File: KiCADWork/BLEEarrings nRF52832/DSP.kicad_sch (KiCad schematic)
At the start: 26 parts, among them J1 Screw_Terminal_01x01, J2 Screw_Terminal_01x02, U2 nRF52832-QFxx, Y1 Crystal_GND23

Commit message: Small Bits
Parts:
- added C14: 100n, Capacitor_SMD:C_0402_1005Metric_Pad0.74x0.62mm_HandSolder, symbol Device:C
- added C15, C16: 16p, Capacitor_SMD:C_0402_1005Metric_Pad0.74x0.62mm_HandSolder, symbol Device:C
- added R8: 2k, Resistor_SMD:R_0402_1005Metric_Pad0.72x0.64mm_HandSolder, symbol Device:R
- added SW2: SW_DIP_x01, easyeda2kicad:KEY-SMD_L3.0-W2.5-LS4.0, symbol Switch:SW_DIP_x01
- added Y2: Crystal, easyeda2kicad:CRYSTAL-SMD_L1.6-W1.0, symbol Device:Crystal
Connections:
- net +3V3: now also R8.2
- net GND: now also C3.1, C4.1, C14.1, C15.1, C16.1, SW2.2; no longer C3.2, C4.2
- net at U2.34 (XC1), Y1.4: now also C3.2; no longer C3.1
- net at U2.35 (XC2), Y1.1: now also C4.2; no longer C4.1
- net at U2.2 (P0.00/XL1): now also C15.2, Y2.2
- net at U2.3 (P0.01/XL2): now also C16.2, Y2.1
- net at U2.42 (P0.30/AIN6): now also C14.2, R8.1, SW2.1
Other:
- moved on the sheet: C3, C4, J1, J2, R5, TP4

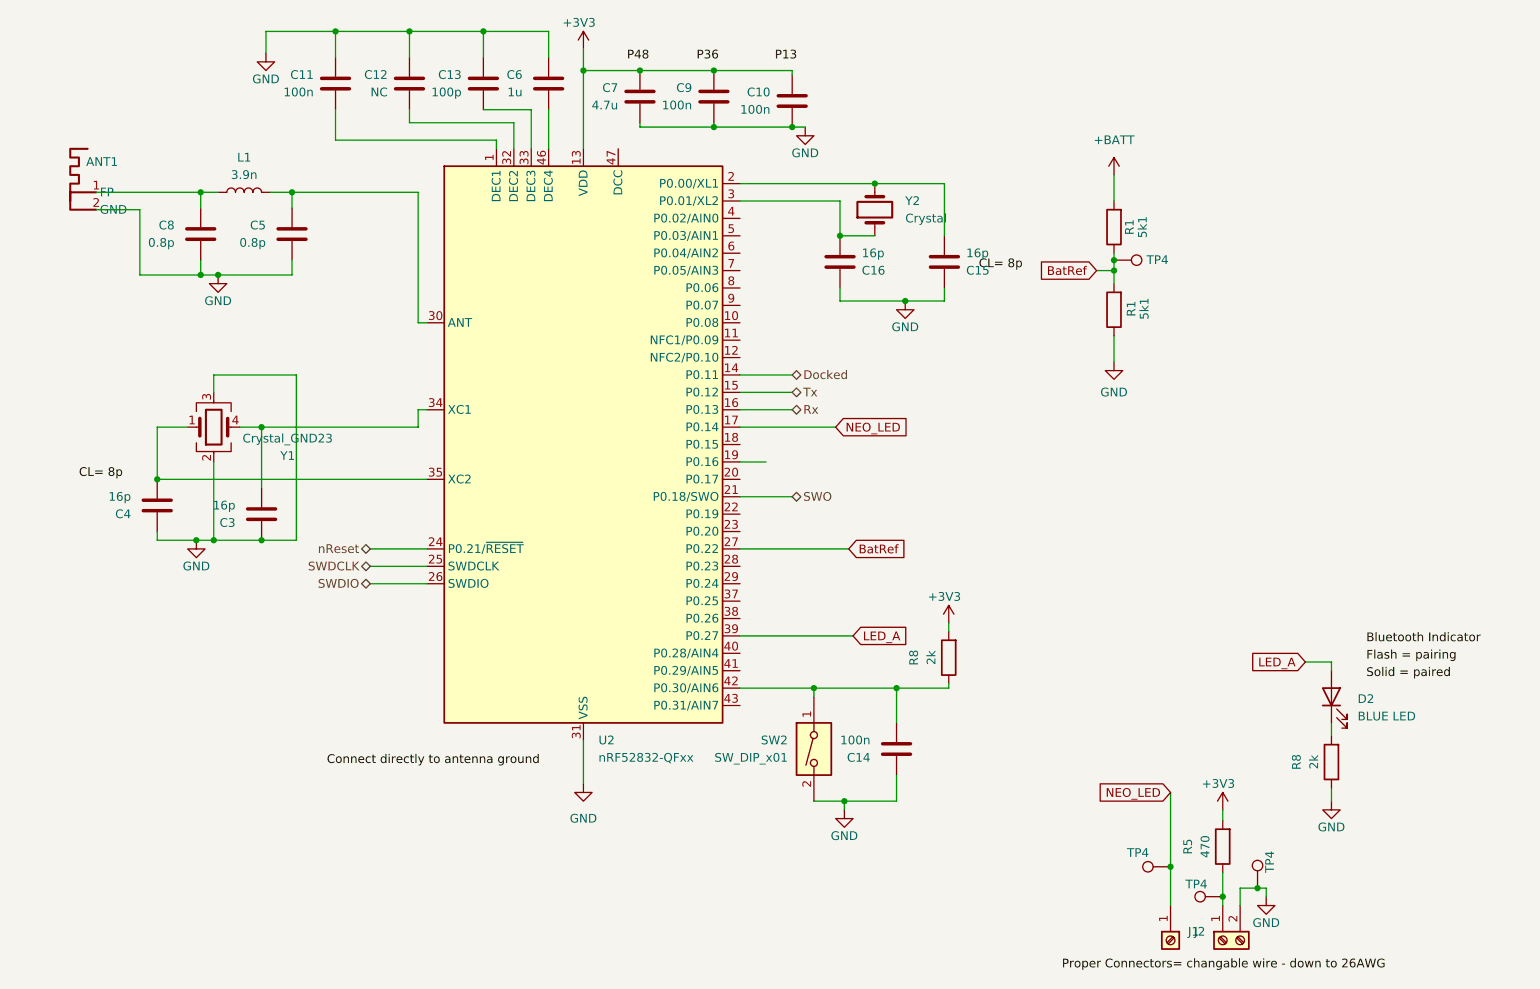
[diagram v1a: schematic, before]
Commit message: New Chip NRF52833
large changes
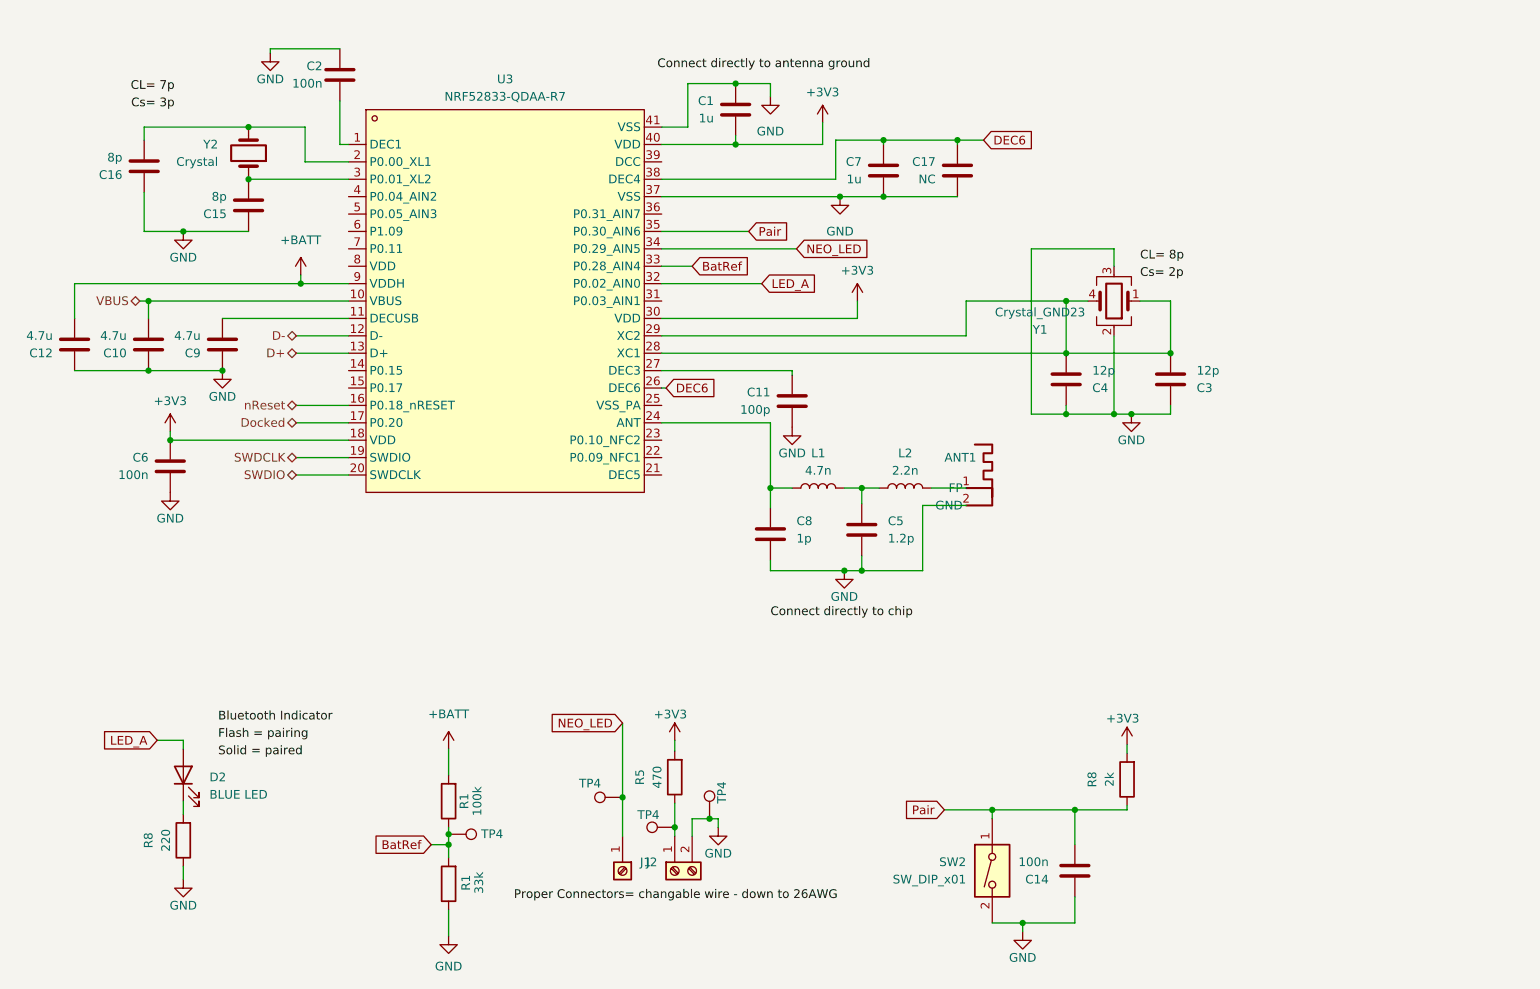
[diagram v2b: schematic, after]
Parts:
- removed C13: 100p, Capacitor_SMD:C_0402_1005Metric_Pad0.74x0.62mm_HandSolder, symbol Device:C
- removed U2: nRF52832-QFxx, Package_DFN_QFN:QFN-48-1EP_6x6mm_P0.4mm_EP4.6x4.6mm, symbol MCU_Nordic:nRF52832-QFxx
- added C1: 1u, Capacitor_SMD:C_0402_1005Metric_Pad0.74x0.62mm_HandSolder, symbol Device:C
- added C17: NC, Capacitor_SMD:C_0402_1005Metric_Pad0.74x0.62mm_HandSolder, symbol Device:C
- added C2: 100n, Capacitor_SMD:C_0402_1005Metric_Pad0.74x0.62mm_HandSolder, symbol Device:C
- added L2: 2.2n, Inductor_SMD:L_0402_1005Metric_Pad0.77x0.64mm_HandSolder, symbol Device:L
- added U3: NRF52833-QDAA-R7, easyeda2kicad:QFN-40_L5.0-W5.0-P0.40-TL-EP3.6, symbol easyeda2kicad:NRF52833-QDAA-R7
- C10, C9: value 100n -> 4.7u
- C11: value 100n -> 100p
- C12: value NC -> 4.7u
- C15, C16: value 16p -> 8p
- C3, C4: value 16p -> 12p
- C5: value 0.8p -> 1.2p
- C6: value 1u -> 100n
- C7: value 4.7u -> 1u
- C8: value 0.8p -> 1p
- L1: value 3.9n -> 4.7n
- R1: value 5k1 -> 33k
- R1: value 5k1 -> 100k
- R8: value 2k -> 220
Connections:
- net +3V3: now also C6.1, C1.2, U3.18 (VDD), U3.30 (VDD), U3.40 (VDD); no longer C10.2, C7.1, C9.2
- net +BATT: now also C12.2, U3.9 (VDDH)
- net BatRef: now also U3.33 (P0.28_AIN4)
- net Docked: now also U3.17 (P0.20)
- net GND: now also C11.2, C6.2, C1.1, C17.2, C2.1, U3.37 (VSS), U3.41 (VSS); no longer C11.1, C6.1
- net LED_A: now also U3.32 (P0.02_AIN0)
- net NEO_LED: now also U3.34 (P0.29_AIN5)
- net SWDCLK: now also U3.19 (SWDIO)
- net SWDIO: now also U3.20 (SWDCLK)
- net nReset: now also U3.16 (P0.18_nRESET)
- net at C15.2: now also Y2.1, U3.3 (P0.01_XL2); no longer Y2.2
- net at C5.1: now also L1.2, L2.1; no longer L1.1
- net at C3.2, Y1.4: now also C4.2, Y1.1, U3.28 (XC1), U3.29 (XC2)
- net Pair: now reaches C14.2, R8.1, SW2.1
- net Pair: now also U3.35 (P0.30_AIN6)
- net at C16.2: now also Y2.2, U3.2 (P0.00_XL1); no longer Y2.1
- new net: C8.1, L1.1, U3.24 (ANT)
- new net: ANT1.1 (FP), L2.2
- new net: C9.2, U3.11 (DECUSB)
- new net: C2.2, U3.1 (DEC1)
- new net: C11.1, U3.27 (DEC3)
- new net D+: U3.13 (D+)
- new net D-: U3.12 (D-)
- new net DEC6: C17.1, C7.1, U3.26 (DEC6), U3.38 (DEC4)
- new net VBUS: C10.2, U3.10 (VBUS)
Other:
- moved on the sheet: D2, J1, J2, R1, R5, R8, TP4

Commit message: Dock Updates
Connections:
- net Docked renamed SWO
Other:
- moved on the sheet: C14, R8, SW2

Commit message: Dock Updates
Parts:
- Y1: value Crystal_GND23 -> XL7EL89CKI-111YLC-32M
- Y2: value Crystal -> X161032768KLD2SI
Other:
- moved on the sheet: C16
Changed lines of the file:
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@@
     (stroke (width 0) (type default))
   )
-  (wire (pts (xy 34.925 40.005) (xy 34.925 41.91))
+  (wire (pts (xy 23.495 40.005) (xy 23.495 41.91))
     (stroke (width 0) (type default))
   )
@@
     (stroke (width 0) (type default))
   )
-  (wire (pts (xy 34.925 40.005) (xy 50.165 40.005))
+  (wire (pts (xy 23.495 40.005) (xy 50.165 40.005))
     (stroke (width 0) (type default))
   )
@@
     (stroke (width 0) (type default))
   )
-  (wire (pts (xy 34.925 55.245) (xy 34.925 49.53))
+  (wire (pts (xy 23.495 55.245) (xy 23.495 49.53))
     (stroke (width 0) (type default))
   )
@@
     (stroke (width 0) (type default))
   )
-  (wire (pts (xy 40.64 55.245) (xy 34.925 55.245))
+  (wire (pts (xy 40.64 55.245) (xy 23.495 55.245))
     (stroke (width 0) (type default))
   )
@@
     (stroke (width 0) (type default))
   )
-  (label "CL= 7p" (at 39.37 34.925 180) (fields_autoplaced)
-    (effects (font (size 1.27 1.27)) (justify right bottom))
-  )
-  (label "Cs= 3p" (at 39.37 37.465 180) (fields_autoplaced)
-    (effects (font (size 1.27 1.27)) (justify right bottom))
+  (label "CL= 7p" (at 27.305 35.56 0) (fields_autoplaced)
+    (effects (font (size 1.27 1.27)) (justify left bottom))
+  )
+  (label "Cs= 3p" (at 27.305 38.1 0) (fields_autoplaced)
+    (effects (font (size 1.27 1.27)) (justify left bottom))
   )
   (label "Connect directly to chip" (at 126.365 111.76 0) (fields_autoplaced)
     (effects (font (size 1.27 1.27)) (justify left bottom))
   )
-  (label "Cs= 2p" (at 180.34 62.23 0) (fields_autoplaced)
+  (label "Cs= 2p" (at 172.085 56.515 0) (fields_autoplaced)
     (effects (font (size 1.27 1.27)) (justify left bottom))
   )
@@
     (effects (font (size 1.27 1.27)) (justify left bottom))
   )
+  (label "32.768kHz Clock" (at 27.305 33.02 0) (fields_autoplaced)
+    (effects (font (size 1.27 1.27)) (justify left bottom))
+  )
   (label "Connect directly to antenna ground" (at 109.855 31.75 0) (fields_autoplaced)
     (effects (font (size 1.27 1.27)) (justify left bottom))
   )
-  (label "CL= 8p" (at 180.34 59.69 0) (fields_autoplaced)
+  (label "CL= 8p" (at 172.085 53.975 0) (fields_autoplaced)
+    (effects (font (size 1.27 1.27)) (justify left bottom))
+  )
+  (label "32MHz clock" (at 172.085 51.435 0) (fields_autoplaced)
     (effects (font (size 1.27 1.27)) (justify left bottom))
   )
@@
       (effects (font (size 1.27 1.27)) (justify right))
     )
-    (property "Value" "Crystal" (at 45.72 45.085 90)
+    (property "Value" " X161032768KLD2SI" (at 45.72 45.085 90)
       (effects (font (size 1.27 1.27)) (justify right))
     )
@@
     )
   )
-  (symbol (lib_id "Device:C") (at 34.925 45.72 180) (unit 1)
-    (in_bom yes) (on_board yes) (dnp no)
-    (property "Reference" "C16" (at 31.75 46.99 0)
-      (effects (font (size 1.27 1.27)) (justify left))
-    )
-    (property "Value" "8p" (at 31.75 44.45 0)
-      (effects (font (size 1.27 1.27)) (justify left))
-    )
-    (property "Footprint" "Capacitor_SMD:C_0402_1005Metric_Pad0.74x0.62mm_HandSolder" (at 33.9598 41.91 0)
-      (effects (font (size 1.27 1.27)) hide)
-    )
-    (property "Datasheet" "~" (at 34.925 45.72 0)
+  (symbol (lib_id "Device:C") (at 23.495 45.72 180) (unit 1)
+    (in_bom yes) (on_board yes) (dnp no)
+    (property "Reference" "C16" (at 20.32 46.99 0)
+      (effects (font (size 1.27 1.27)) (justify left))
+    )
+    (property "Value" "8p" (at 20.32 44.45 0)
+      (effects (font (size 1.27 1.27)) (justify left))
+    )
+    (property "Footprint" "Capacitor_SMD:C_0402_1005Metric_Pad0.74x0.62mm_HandSolder" (at 22.5298 41.91 0)
+      (effects (font (size 1.27 1.27)) hide)
+    )
+    (property "Datasheet" "~" (at 23.495 45.72 0)
       (effects (font (size 1.27 1.27)) hide)
     )
@@
   )
   (symbol (lib_id "Device:Crystal_GND23") (at 176.53 65.405 180) (unit 1)
-    (in_bom yes) (on_board yes) (dnp no) (fields_autoplaced)
-    (property "Reference" "Y1" (at 165.735 69.5959 0)
-      (effects (font (size 1.27 1.27)))
-    )
-    (property "Value" "Crystal_GND23" (at 165.735 67.0559 0)
-      (effects (font (size 1.27 1.27)))
-    )
+    (in_bom yes) (on_board yes) (dnp no)
+    (property "Reference" "Y1" (at 182.245 63.5 0)
+      (effects (font (size 1.27 1.27)))
+    )
+    (property "Value" "XL7EL89CKI-111YLC-32M " (at 193.675 60.96 0)
+      (effects (font (size 1.27 1.27)))
+    )

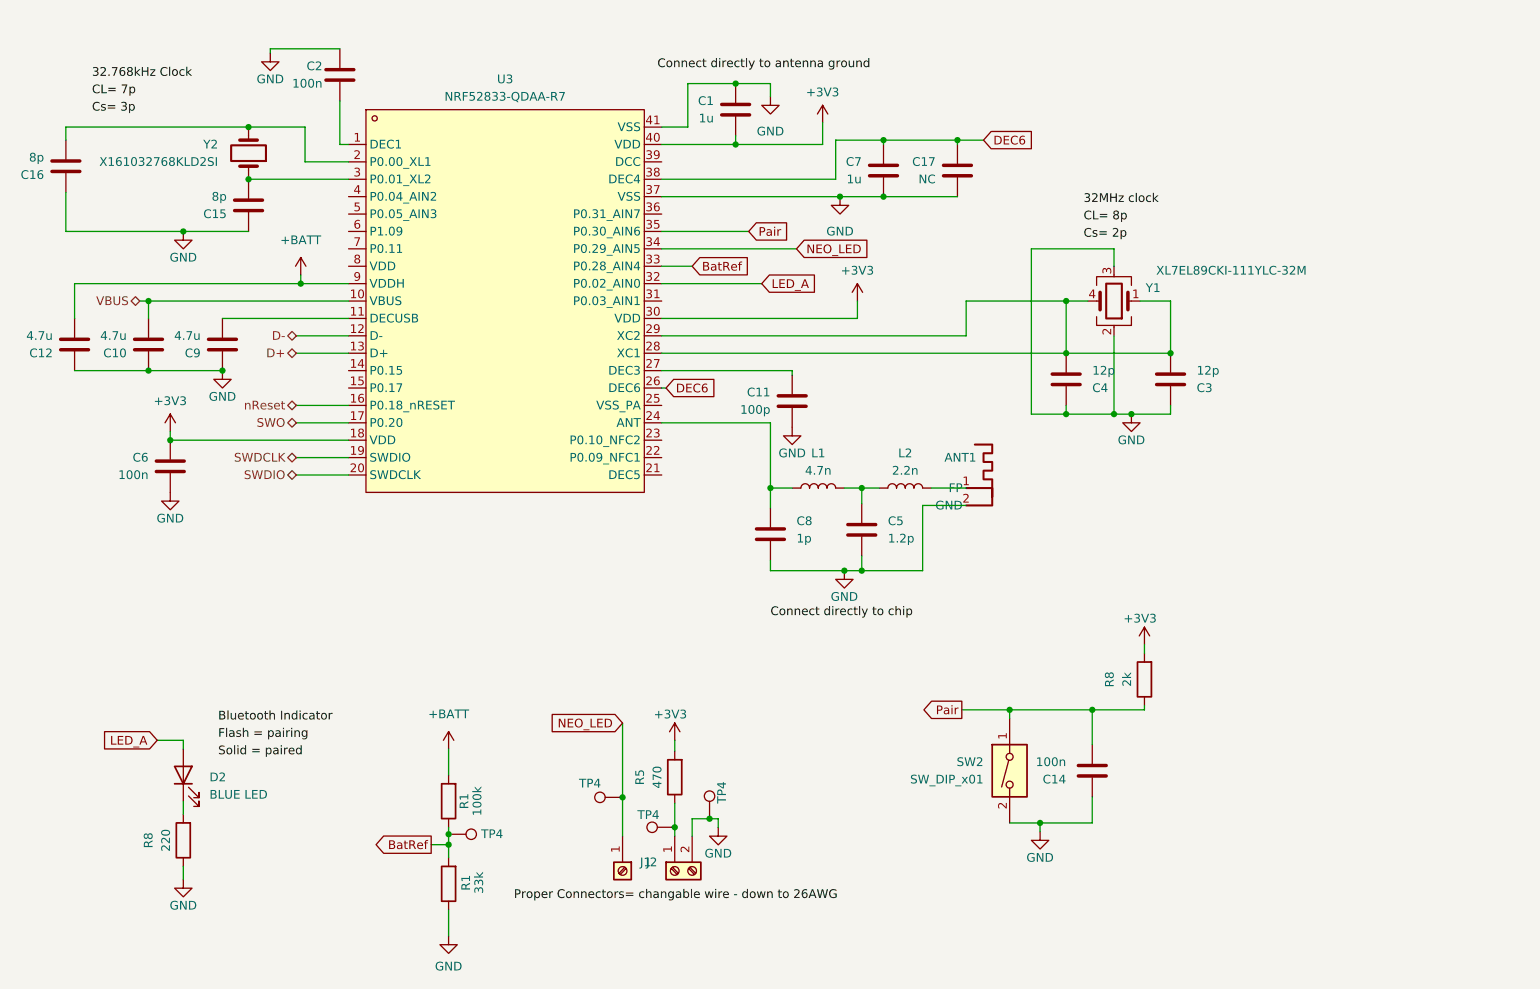
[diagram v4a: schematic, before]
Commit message: Routing Started on Earrings Again
- Only small routing changes made
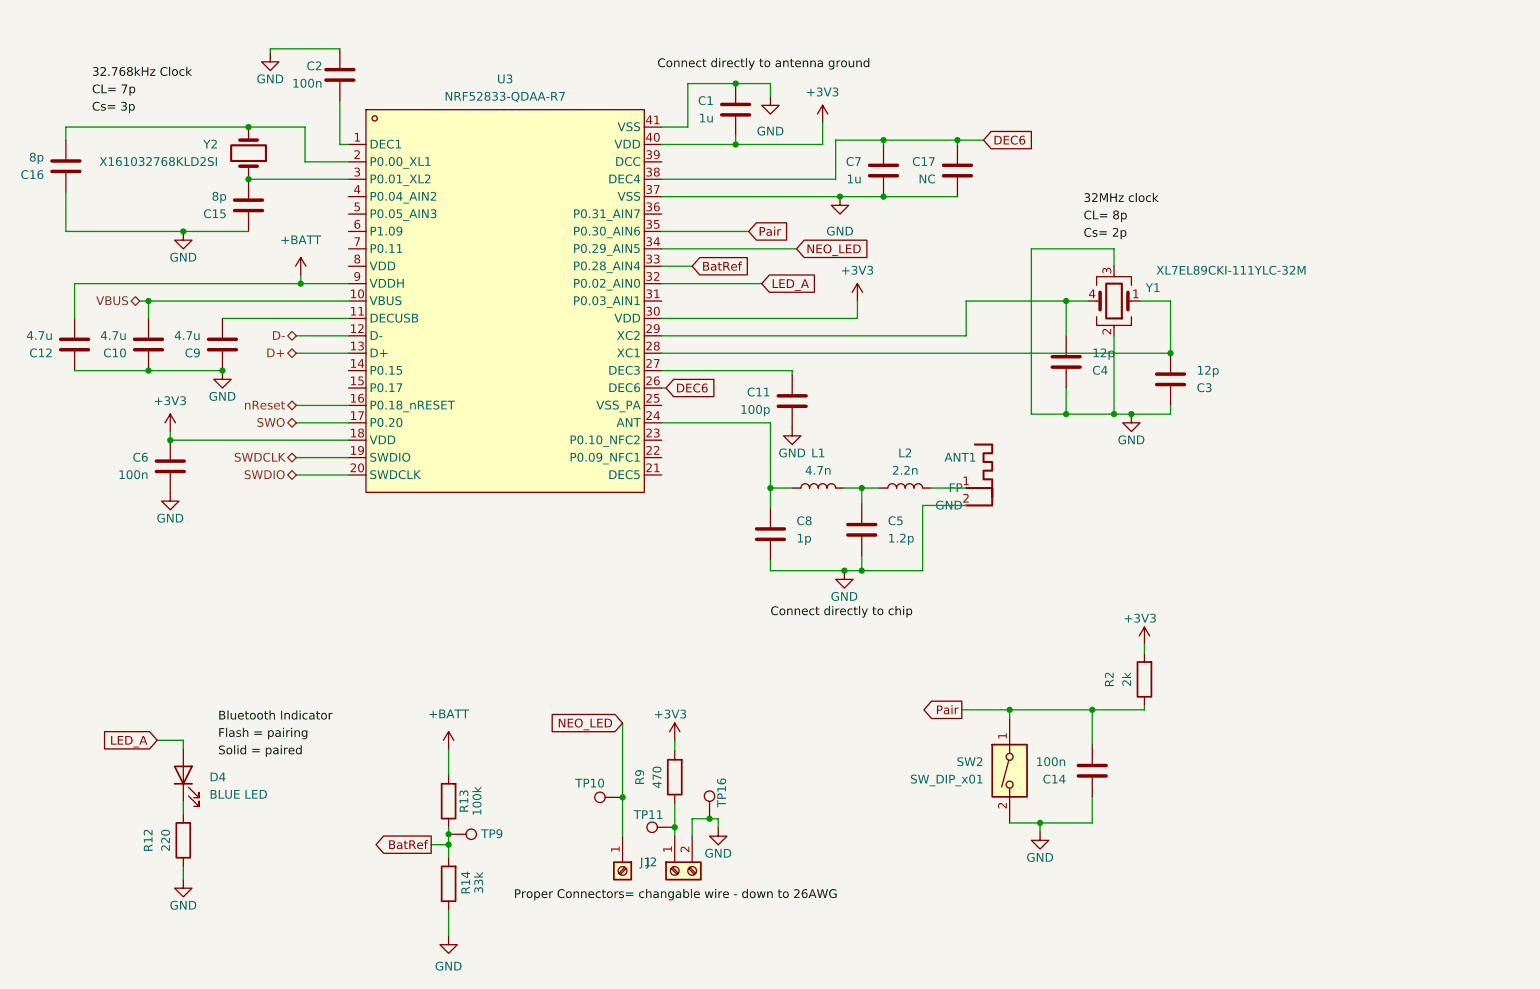
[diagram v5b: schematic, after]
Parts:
- renumbered D2 to D4, R8 to R12, R1 to R13, R1 to R14, R8 to R2, R5 to R9, TP4 to TP10, TP4 to TP11, TP4 to TP16, TP4 to TP9
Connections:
- net at C4.2, U3.29 (XC2), Y1.4: no longer C3.2, U3.28 (XC1), Y1.1
- new net: C3.2, U3.28 (XC1), Y1.1
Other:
- moved on the sheet: C4

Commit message: Ignoring Backups
More Dock progress
All local backups removed
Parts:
- added R5, R6, R7, R8: NF, Resistor_SMD:R_0201_0603Metric, symbol Device:R
- ANT1, C17: LCSC Part (none) -> N/A
- C1, C7: LCSC Part (none) -> C14445
- C10, C12, C9: LCSC Part (none) -> C307423
- C11: LCSC Part (none) -> C5137573
- C14, C2, C6: LCSC Part (none) -> C60474
- C15, C16: LCSC Part (none) -> C5448809
- C3, C4: LCSC Part (none) -> C696888
- C5: LCSC Part (none) -> C880658
- C8: LCSC Part (none) -> C880647
- D2: renamed from D4; LCSC Part (none) -> C7371904
- J1: LCSC Part (none) -> C2765059
- J2: LCSC Part (none) -> C2765060
- L1: LCSC Part (none) -> C13595
- L2: LCSC Part (none) -> C395061
- R1: renamed from R14; LCSC Part (none) -> C138003
- R1: renamed from R13; LCSC Part (none) -> C60491
- R5: renamed from R9; LCSC Part (none) -> C114949
- R8: renamed from R2; LCSC Part (none) -> C60488
- R8: renamed from R12; LCSC Part (none) -> C112291
- SW2: LCSC Part (none) -> C2905194
- TP4: renamed from TP10; LCSC Part (none) -> N/A
- TP4: renamed from TP11; LCSC Part (none) -> N/A
- TP4: renamed from TP9; LCSC Part (none) -> N/A
- TP4: renamed from TP16; LCSC Part (none) -> N/A
- Y1: LCSC Part (none) -> C2965582
- Y2: LCSC Part (none) -> C383846
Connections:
- net BatRef: now also U3.34 (P0.29_AIN5); no longer U3.33 (P0.28_AIN4)
- net NEO_LED: now also U3.33 (P0.28_AIN4); no longer U3.34 (P0.29_AIN5)
- net SWDCLK: now also R8.1; no longer U3.19 (SWDIO)
- net SWDIO: now also R7.2; no longer U3.20 (SWDCLK)
- net SWO: now also R6.2; no longer U3.17 (P0.20)
- net nReset: now also R5.1; no longer U3.16 (P0.18_nRESET)
- new net: R6.1, U3.17 (P0.20)
- new net: R7.1, U3.20 (SWDCLK)
- new net: R8.2, U3.19 (SWDIO)
- new net: R5.2, U3.16 (P0.18_nRESET)
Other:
- moved on the sheet: C4
